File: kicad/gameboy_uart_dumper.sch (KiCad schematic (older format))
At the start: 87 parts, among them J1 USB_B, J2 AVR-ISP-6, J3 Game Boy cartridge connector, U1 FT232RL, U2 ATtiny2313V-10PU, U3 74HC595, U4 74HC595, U5 74HC595, U6 74HC165, Y1 10MHz

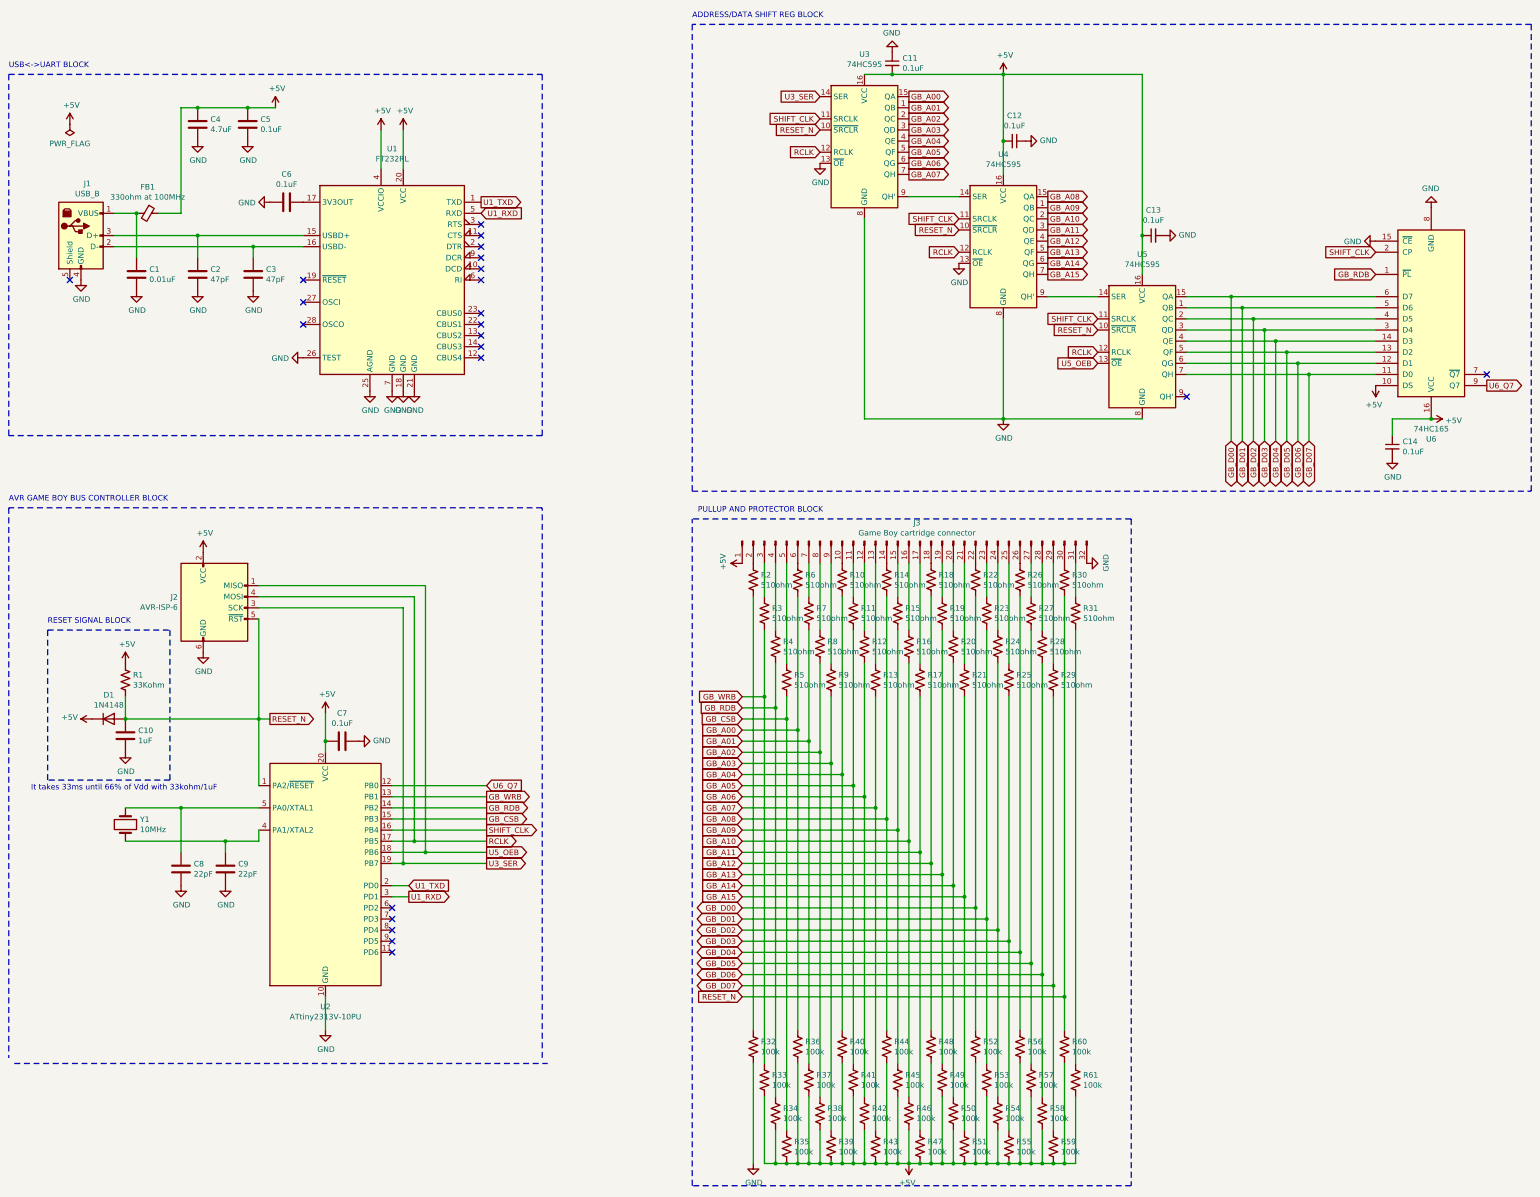
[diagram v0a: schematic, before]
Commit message: Update circuit (divide GB_RDB into GB_RDB and U6_PLB and changed crystal from 10MHz to 18.432MHz) and update firmware and software (transferrate 19.2kbps->430.8kbps. support TAMA5 dumping. fixed global checksum program. )
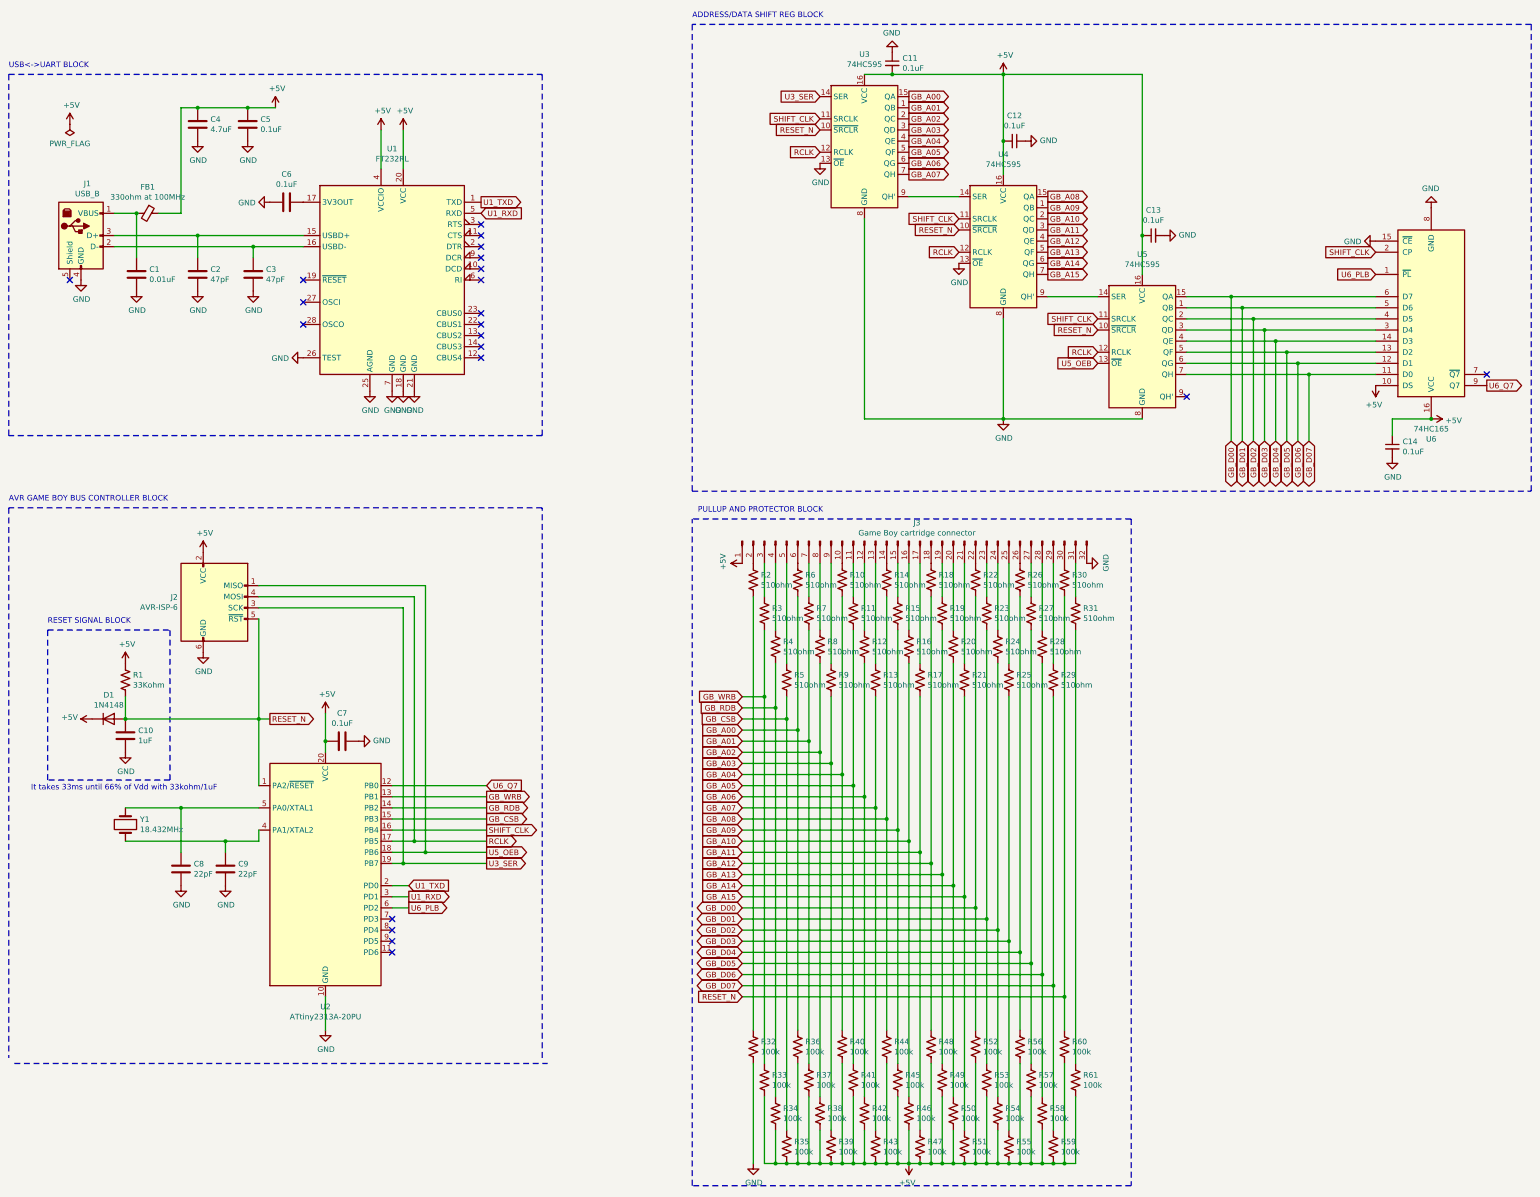
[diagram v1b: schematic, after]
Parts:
- U2: value ATtiny2313V-10PU -> ATtiny2313A-20PU
- Y1: value 10MHz -> 18.432MHz
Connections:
- net GB_RDB: no longer U6.1 (~PL)
- net U6_PLB: now reaches U2.6 (PD2)
- net U6_PLB: now also U6.1 (~PL)
- no-connect marks 22 -> 21
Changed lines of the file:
@@
 Sheet 1 1
 Title ""
-Date "2019-11-29"
-Rev "1.00"
+Date "2020-01-06"
+Rev "1.10"
 Comp ""
 Comment1 ""
@@
 P 4050 8350
 F 0 "U2" H 4050 7161 50  0000 C CNN
-F 1 "ATtiny2313V-10PU" H 4050 7070 50  0000 C CNN
+F 1 "ATtiny2313A-20PU" H 4050 7070 50  0000 C CNN
 F 2 "Package_DIP:DIP-20_W7.62mm" H 4050 8350 50  0001 C CIN
 F 3 "http://ww1.microchip.com/downloads/en/DeviceDoc/Atmel-2543-AVR-ATtiny2313_Datasheet.pdf" H 4050 8350 50  0001 C CNN
@@
 P 2250 7900
 F 0 "Y1" V 2204 8031 50  0000 L CNN
-F 1 "10MHz" V 2295 8031 50  0000 L CNN
+F 1 "18.432MHz" V 2295 8031 50  0000 L CNN
 F 2 "" H 2250 7900 50  0001 C CNN
 F 3 "~" H 2250 7900 50  0001 C CNN
@@
 Wire Wire Line
 	4650 8550 4800 8550
-NoConn ~ 4650 8650
 NoConn ~ 4650 8750
 NoConn ~ 4650 8850
@@
 SHIFT_CLK
 Text GLabel 13500 2950 0    50   Input ~ 0
-GB_RDB
+U6_PLB
 Text GLabel 14500 3950 2    50   Output ~ 0
 U6_Q7
@@
 	1    0    0    -1
 $EndComp
+Text GLabel 4800 8650 2    50   Output ~ 0
+U6_PLB
+Wire Wire Line
+	4650 8650 4800 8650
 $EndSCHEMATC
